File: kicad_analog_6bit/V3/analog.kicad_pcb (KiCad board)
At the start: 2 copper layers, 50 x 23.2 mm, 30 parts, among them P1 Conn_02x05_Odd_Even, P2 Conn_01x04, P3 Conn_01x06, P4 Conn_01x02, P6 Conn_01x01, P7 Conn_01x01, U1 MAX9144, U2 MAX9144, U3 4066, U4 MAX5259EEE+, U5 MCP1754S-3302xCB

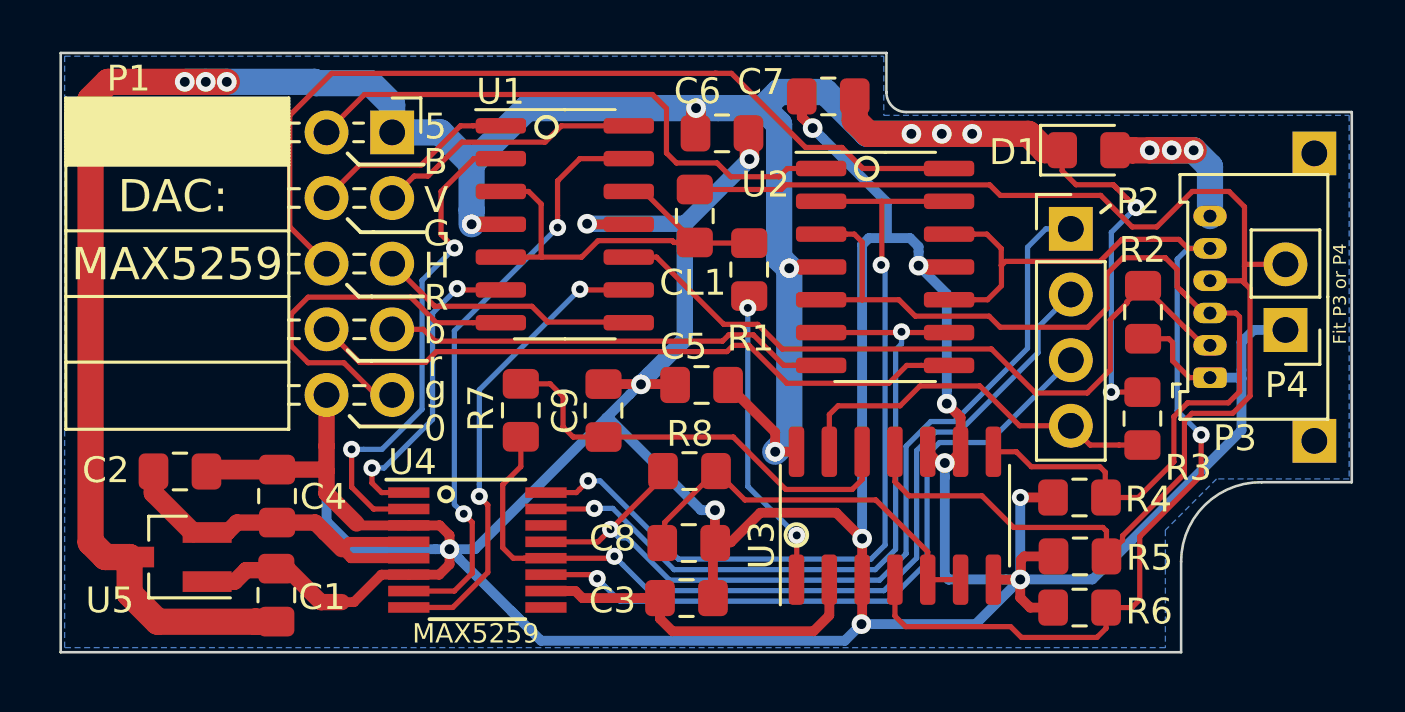
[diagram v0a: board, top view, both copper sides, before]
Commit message: Update issue 3 with normally closed DG441
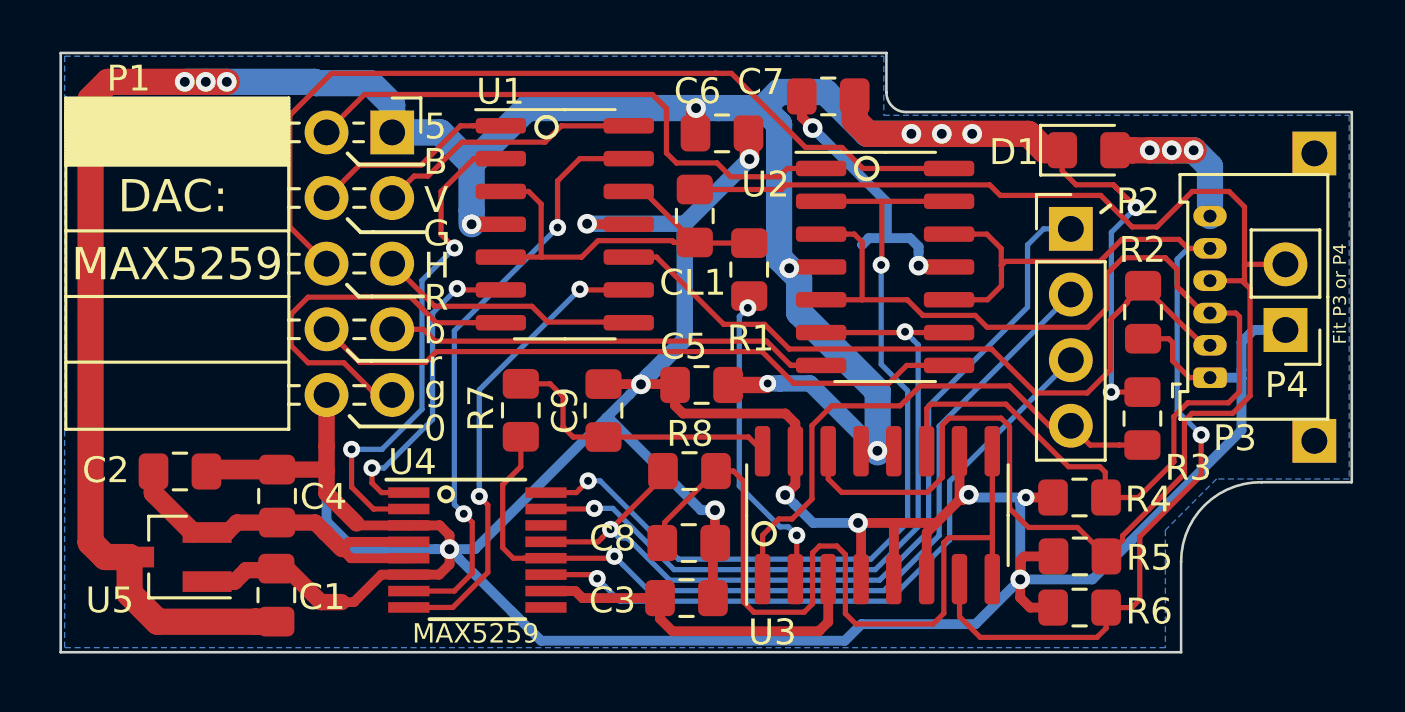
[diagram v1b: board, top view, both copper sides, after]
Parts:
- R7, R8: value 100K -> 10K
- U3: value 4066 -> DG441xY; footprint Package_SO:SOIC-14_3.9x8.7mm_P1.27mm -> Package_SO:SOIC-16_3.9x9.9mm_P1.27mm
- moved U3 0.68 mm to (59.1, 49.2)
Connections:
- U3 pad 1: /SW_CLAMP -> /CLAMP
- U3 pad 11: /AGREEN -> /ABLUE
- U3 pad 12: /TERM_G -> /VCC
- U3 pad 13: /CLAMP -> /VCC
- U3 pad 14: /VCC -> /AGREEN
- U3 pad 2: /CLAMPLVL -> /SW_CLAMP
- U3 pad 3: /GND -> /CLAMPLVL
- U3 pad 4: /ARED -> /GND
- U3 pad 5: /TERM_RB -> /GND
- U3 pad 6: /TERM_RB -> /GND
- U3 pad 7: /GND -> /ARED
- U3 pad 8: /ABLUE -> /TERM_RB
- U3 pad 9: /GND -> /TERM_RB
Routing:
- net /TERM_RB: track 15.5 -> 32.1 mm
- net /GND: track 181.4 -> 168.8 mm, vias 13 -> 12
- net /AGREEN: track 54.0 -> 61.4 mm
- net /CLAMP: track 15.0 -> 21.4 mm
- net /TERM_G: track 16.8 -> 11.1 mm
- net /ABLUE: track 41.3 -> 46.4 mm
- net /VCC: track 113.1 -> 117.8 mm, vias 12 -> 13
- net /ARED: track 45.0 -> 42.6 mm
- net /GPIO22_STB: track 27.0 -> 25.9 mm
- net /REFRBUVHI: track 33.1 -> 33.8 mm
- net /REFRBUVLO: track 28.4 -> 29.0 mm
- net /GPIO1_CLK: track 35.9 -> 35.4 mm

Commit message: Analog V3 non-inverted 14 pin
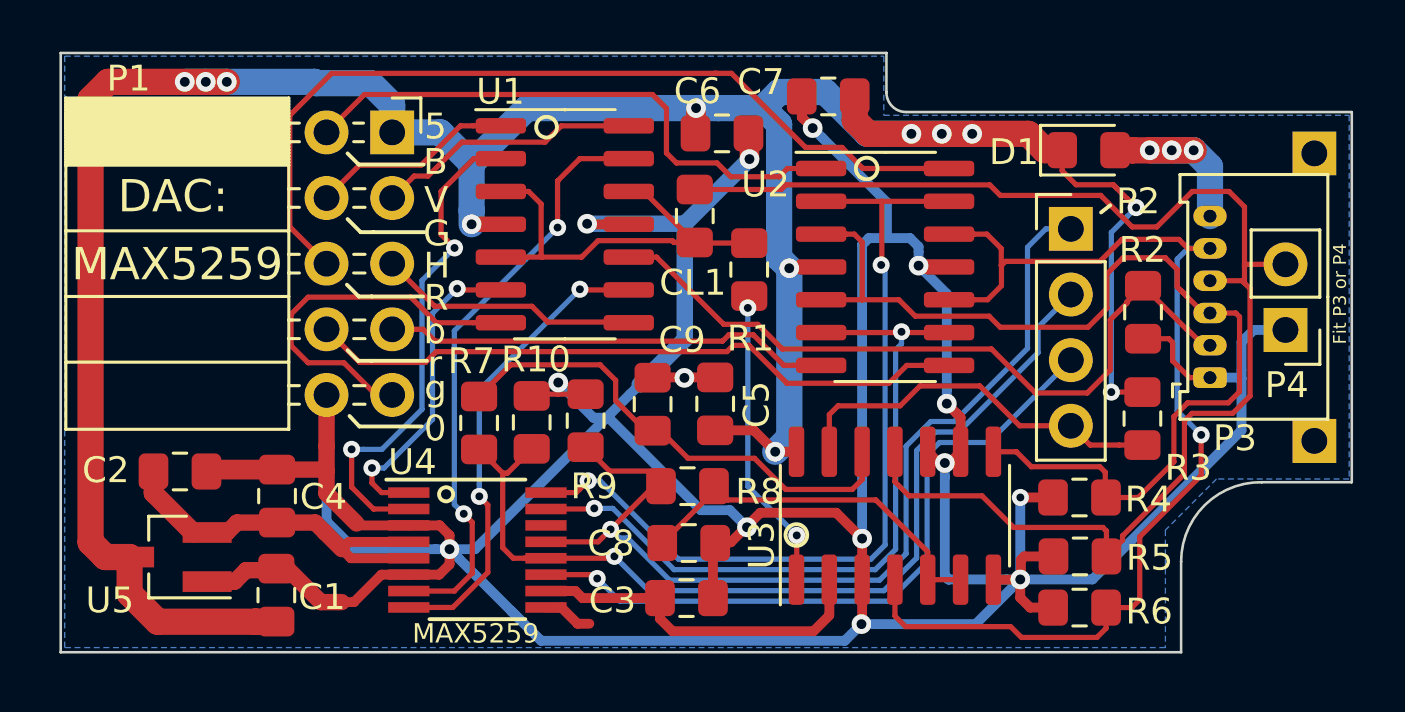
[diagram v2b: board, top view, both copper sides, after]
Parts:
- added R10: 1K, Resistor_SMD:R_0805_2012Metric_Pad1.15x1.40mm_HandSolder, F.Cu at (45.8, 45.6)
- added R9: 1K, Resistor_SMD:R_0805_2012Metric_Pad1.15x1.40mm_HandSolder, F.Cu at (47.8, 45.5)
- R1: value 150R -> 75R
- U3: value DG441xY -> 4066; footprint Package_SO:SOIC-16_3.9x9.9mm_P1.27mm -> Package_SO:SOIC-14_3.9x8.7mm_P1.27mm
- moved C9 1.92 mm to (50.4, 44.9)
- moved R7 1.69 mm to (43.7, 45.6)
- moved C5 0.90 mm to (52.9, 44.9), turned to 90 degrees
- moved U3 0.68 mm to (59.8, 49.2)
- moved R8 0.59 mm to (51.8, 48.1)
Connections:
- U3 pad 1: /CLAMP -> /SW_CLAMP
- U3 pad 11: /ABLUE -> /AGREEN
- U3 pad 12: /VCC -> /TERM_G
- U3 pad 13: /VCC -> /CLAMP
- U3 pad 14: /AGREEN -> /VCC
- U3 pad 2: /SW_CLAMP -> /CLAMPLVL
- U3 pad 3: /CLAMPLVL -> /GND
- U3 pad 4: /GND -> /ARED
- U3 pad 5: /GND -> /TERM_RB
- U3 pad 6: /GND -> /TERM_RB
- U3 pad 7: /ARED -> /GND
- U3 pad 8: /TERM_RB -> /ABLUE
- U3 pad 9: /TERM_RB -> /GND
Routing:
- net /GND: track 168.8 -> 186.7 mm, vias 12 -> 14
- net /TERM_RB: track 32.1 -> 14.5 mm
- net /TERM_G: track 11.1 -> 19.2 mm
- net /AGREEN: track 61.4 -> 54.0 mm
- net /CLAMP: track 21.4 -> 15.0 mm
- net /VCC: track 117.8 -> 112.3 mm, vias 13 -> 12
- net /ABLUE: track 46.4 -> 41.3 mm
- net /GPIO0_DAT: track 34.3 -> 38.2 mm
- net /ARED: track 42.6 -> 45.0 mm
- net /SPARE: track 0.00 -> 1.94 mm
- net /GPIO1_CLK: track 35.4 -> 37.0 mm
- net /GPIO22_STB: track 25.9 -> 27.0 mm
- net /REFRBUVHI: track 33.8 -> 33.1 mm
- net /REFRBUVLO: track 29.0 -> 28.4 mm

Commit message: V3 PCB layout with MAX4610
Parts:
- added J1: Spare DAC, TestPoint:TestPoint_Pad_D1.0mm, F.Cu at (48.8, 53.4)
- U1, U2: value MAX9144 -> MAX9108
- U3: value 4066 -> MAX4610
- renumbered C8 to C4, C9 to C5, C5 to C7, C7 to C8, C4 to C9, CL1 to Cx1, R3 to R1, R9 to R3, R10 to R4, R8 to R5, R7 to R6, R4 to R7, R5 to R8, R6 to R9, R1 to Rx1
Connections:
- R3 pad 1: /GPIO0_DAT -> /GPIO1_CLK
- R4 pad 1: /GPIO1_CLK -> /GPIO0_DAT
- R5 pad 2: /GPIO0_DAT -> /GPIO1_CLK
- R6 pad 2: /GPIO1_CLK -> /GPIO0_DAT
- U4 pad 10: /CLAMPLVL -> /SPARE
- U4 pad 9: /SPARE -> /CLAMPLVL
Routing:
- net /SPARE: track 1.94 -> 7.06 mm
- net /GPIO1_CLK: track 37.0 -> 35.5 mm
- net /GPIO0_DAT: track 38.2 -> 38.8 mm
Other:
- board text added: "MAX4610"
- board text added: "MAX9108"
- board text removed: "DAC:"

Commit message: Update pcb with AC/DC switch
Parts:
- removed the C5 at (50.4, 44.9)
- removed the R4 at (45.8, 45.6)
- removed the R6 at (43.7, 45.6)
- added U6: TS5A3159ADBVR, Package_TO_SOT_SMD:SOT-23-6_Handsoldering, F.Cu at (46.3, 45.4)
- moved R3 2.80 mm to (50.6, 44.9)
- renumbered Cx1 to C1, C6 to C2, C7 to C3, C8 to C4, C9 to C5, C1 to C6, C2 to C7, C3 to C8, C4 to C9, Rx1 to R1, R1 to R4, R7 to R6, R8 to R7, R9 to R8
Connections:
- net /SW_CLAMP renamed /VCLAMP
- C9 pad 1: /TERM_RB -> /TERM
- R5 pad 1: /TERM_RB -> /TERM
- U1 pad 12: /CGREEN -> /SGREEN
- U1 pad 3: /CGREEN -> /SGREEN
- U1 pad 5: /CGREEN -> /SGREEN
- U3 pad 12: /TERM_G -> /TERM
- U3 pad 5: /TERM_RB -> /TERM
- U3 pad 6: /TERM_RB -> /TERM
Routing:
- net /SGREEN: track 0.00 -> 20.6 mm, vias 0 -> 2
- net /TERM_G: track 19.2 -> 0.00 mm
- net /TERM: track 0.00 -> 17.6 mm
- net /VCC: track 112.3 -> 129.5 mm, vias 12 -> 13
- net /TERM_RB: track 14.5 -> 0.00 mm
- net /AGREEN: track 54.0 -> 67.7 mm, vias 0 -> 2
- net /GND: track 186.7 -> 178.9 mm
- net /REFSYNC: track 18.2 -> 21.6 mm
- net /GPIO0_DAT: track 38.8 -> 41.4 mm
- net /REFGYLO: track 12.5 -> 13.3 mm
- net /REFGYSYNC: track 23.0 -> 23.7 mm
- net /CGREEN: track 17.3 -> 17.0 mm, vias 0 -> 2
